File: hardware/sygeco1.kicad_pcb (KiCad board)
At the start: 2 copper layers, 57.1 x 33 mm, 12 parts, among them J1 SSD1306_module, SW1 SW_Push_DPDT, SW2 SW_Push_DPDT, U1 ATtiny85-20PU

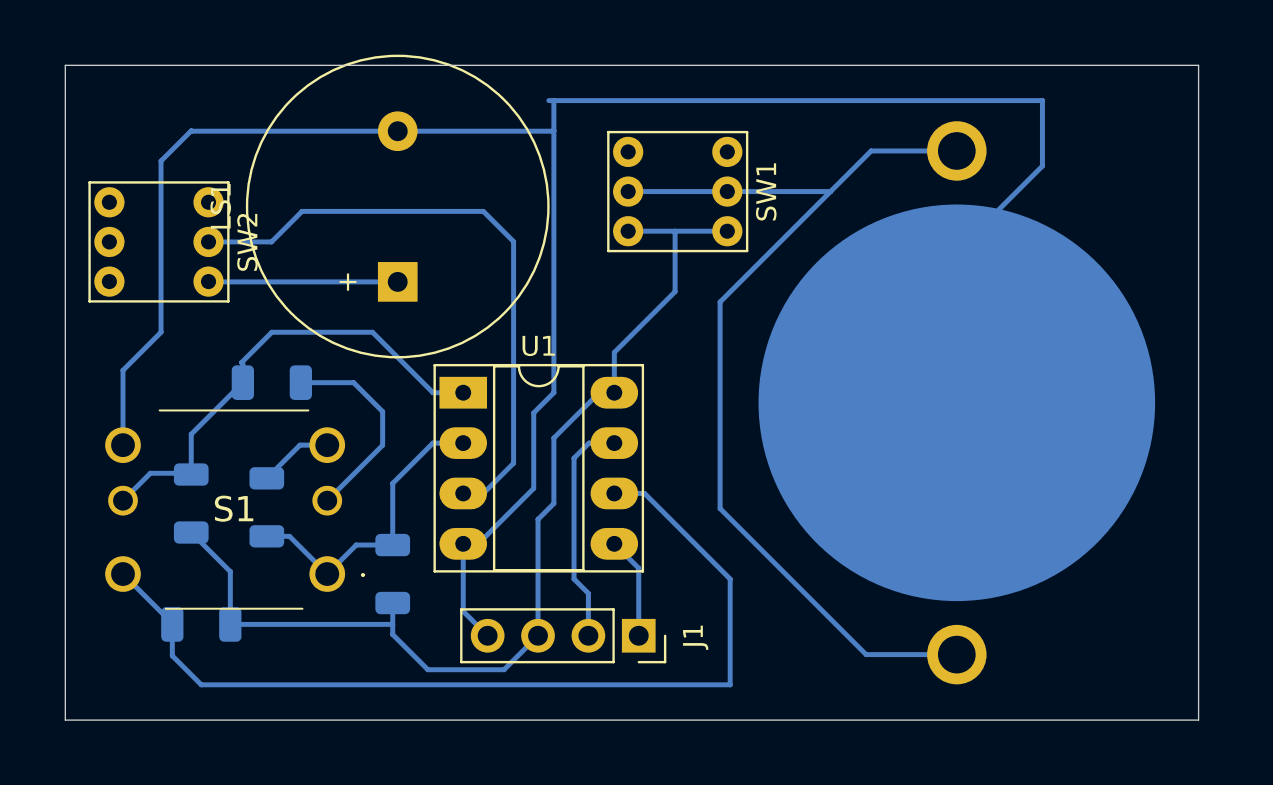
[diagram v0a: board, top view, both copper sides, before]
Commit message: add some text/logo
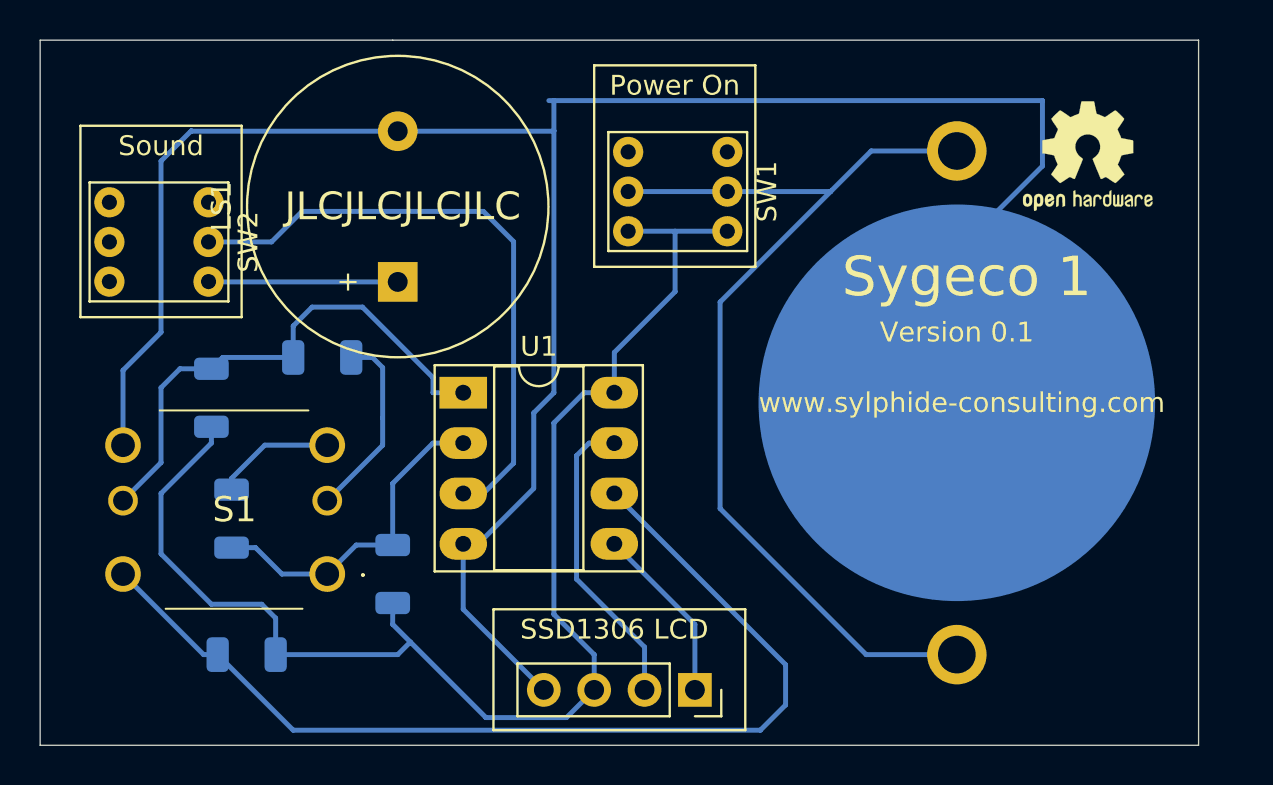
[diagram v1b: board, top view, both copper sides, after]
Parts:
- added REF**: OSHW-Logo2_7.3x6mm_SilkScreen, Symbol:OSHW-Logo2_7.3x6mm_SilkScreen, F.Cu at (177.3, 93.5)
- R3: value 50k -> 33k
- moved R1 5.43 mm to (133.1, 105.7)
- moved J1 3.93 mm to (157.5, 120.4)
- moved R2 2.84 mm to (138.7, 103.6)
- moved R3 2.75 mm to (134.9, 118.6)
- moved R5 1.87 mm to (134.1, 111.8)
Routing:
- net VCC: track 52.7 -> 69.6 mm
- net Button: track 46.9 -> 51.4 mm
- net GND: track 107.9 -> 111.8 mm
- net SDA: track 5.25 -> 9.05 mm
- net SCL: track 11.6 -> 15.4 mm
- net PAD_AXE_1: track 23.9 -> 26.6 mm
- net Net-(R5-Pad2): track 3.74 -> 6.09 mm
- net PAD_AXE_2: track 15.3 -> 16.8 mm
- net Net-(R2-Pad2): track 10.4 -> 9.67 mm
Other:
- board size 57.1 x 33 mm -> 58.4 x 35.6 mm
- board text added: "JLCJLCJLCJLC"
- board text added: "Power On"
- board text added: "SSD1306 LCD"
- board text added: "Sound"
- board text added: "Sygeco 1"
- board text added: "Version 0.1"
- board text added: "www.sylphide-consulting.com"

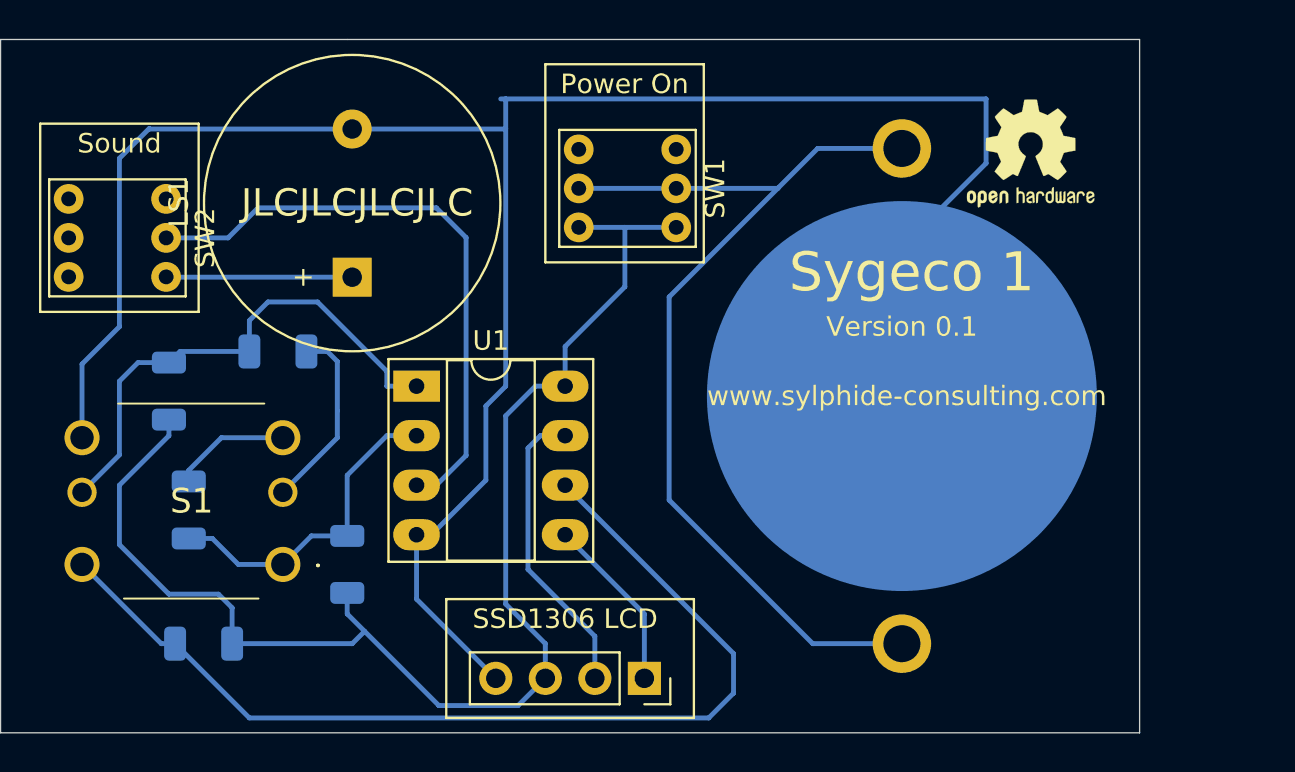
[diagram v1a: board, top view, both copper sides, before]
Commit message: keep on 'improving'. Changed beeper and cell battery holder, according to what i can get my hand on.
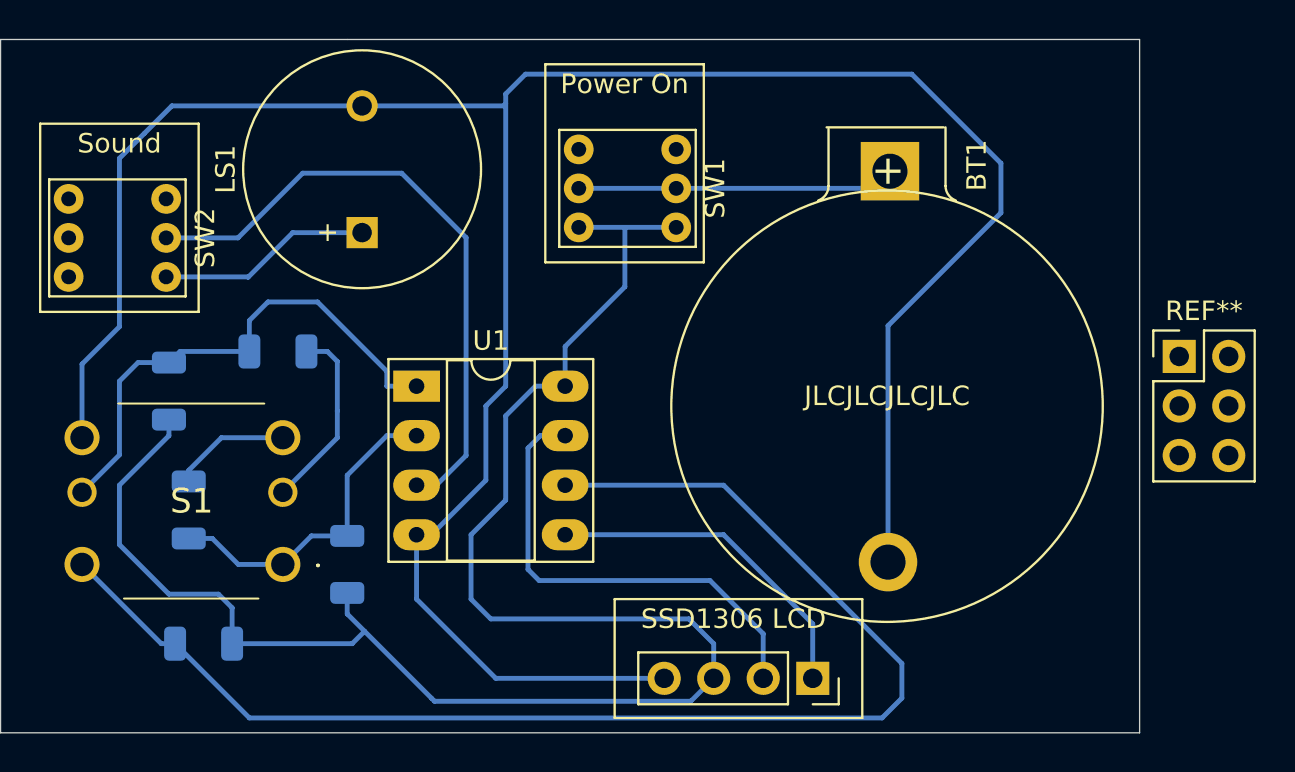
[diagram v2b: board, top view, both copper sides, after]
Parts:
- added G***: LOGO, sygeco:Sylphide_logo, B.Cu at (162.1, 105.9)
- added REF**: PinHeader_2x03_P2.54mm_Vertical, Connector_PinHeader_2.54mm:PinHeader_2x03_P2.54mm_Vertical, F.Cu at (184.9, 103.9)
- BT1: footprint Battery:BatteryHolder_Keystone_3009_1x2450 -> sygeco:BatteryHolder_China_1x20mm; moved to F.Cu
- LS1: footprint Buzzer_Beeper:Buzzer_15x7.5RM7.6 -> Buzzer_Beeper:MagneticBuzzer_ProSignal_ABT-410-RC
- REF**: moved to B.Cu
- moved REF** 23.9 mm to (176.5, 117.3), turned to 180 degrees
- moved BT1 14.8 mm to (169.9, 91.2)
- moved J1 8.64 mm to (166.1, 120.4)
- moved LS1 2.34 mm to (143.0, 97.5)
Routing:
- net Net-(BT1-Pad1): track 50.7 -> 16.3 mm
- net VCC: track 69.6 -> 89.1 mm
- net GND: track 111.8 -> 129.8 mm
- net Button: track 51.4 -> 68.6 mm
- net SCL: track 15.4 -> 24.1 mm
- net SDA: track 9.05 -> 17.4 mm
- net Net-(LS1-Pad1): track 9.55 -> 11.0 mm
- net Net-(SW2-Pad2): track 31.0 -> 32.5 mm

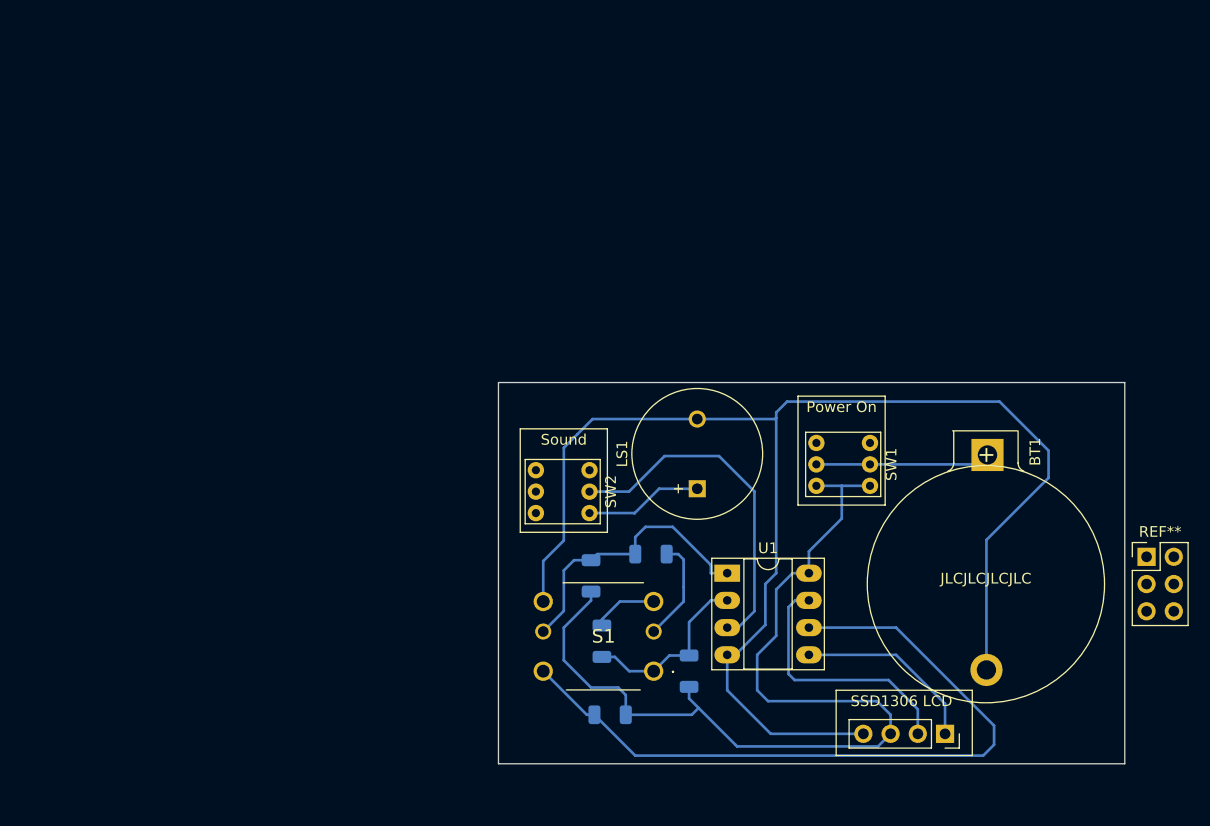
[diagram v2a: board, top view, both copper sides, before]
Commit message: add an ISP header, a power led, and redo completely the routing: * the board is bigger, but hopefully more 'practical' to use * using two layers of copper. it's the same price, why bother ?
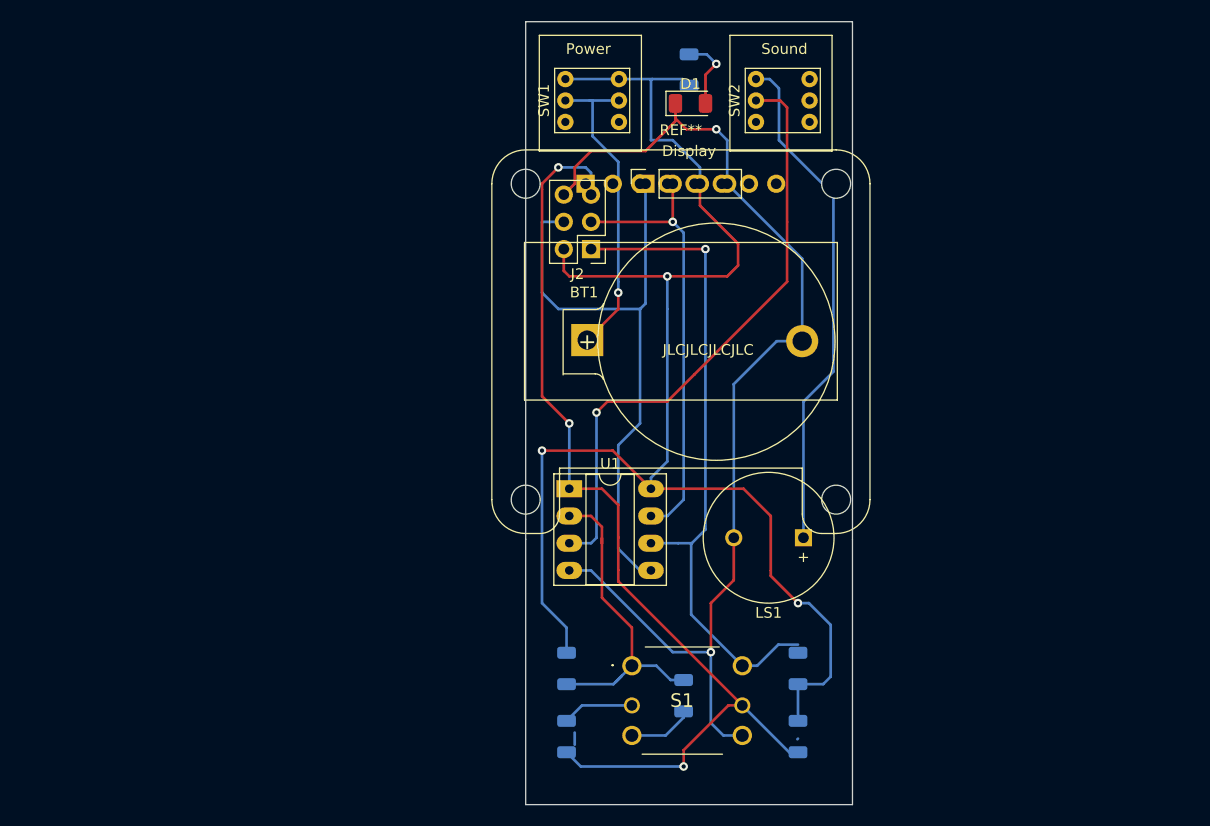
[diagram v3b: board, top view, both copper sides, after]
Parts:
- removed the REF** at (184.9, 103.9)
- added D1: LED, LED_SMD:LED_1206_3216Metric, F.Cu at (142.4, 61.6)
- added J2: AVR-ISP-6, Connector_PinHeader_2.54mm:PinHeader_2x03_P2.54mm_Vertical, F.Cu at (133.1, 75.2)
- added R6: 15, Resistor_SMD:R_1206_3216Metric, B.Cu at (142.2, 58.5)
- added REF**: Adafruit_SSD1306, Display:Adafruit_SSD1306, F.Cu at (132.6, 69.1)
- moved REF** 63.4 mm to (142.2, 64.0), turned to 270 degrees
- moved J1 58.4 mm to (138.2, 69.1), turned to 90 degrees
- moved SW2 51.0 mm to (157.5, 60.3), turned to 90 degrees
- moved BT1 41.1 mm to (129.5, 83.8), turned to 0 degrees
- moved SW1 37.4 mm to (139.7, 60.3), turned to 90 degrees
- moved G*** 33.3 mm to (149.9, 74.9), turned to 270 degrees
- moved R1 24.4 mm to (152.4, 120.7), turned to 270 degrees
- moved R2 18.8 mm to (130.8, 120.7), turned to 90 degrees
- moved R3 18.1 mm to (152.4, 114.3), turned to 90 degrees
- moved U1 16.7 mm to (131.1, 97.5)
- moved R4 11.4 mm to (130.8, 114.3), turned to 270 degrees
- moved LS1 10.9 mm to (152.9, 102.1), turned to 180 degrees
- moved R5 9.16 mm to (141.7, 116.8), turned to 270 degrees
- moved S1 2.09 mm to (136.9, 114.0), turned to 0 degrees
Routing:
- net PAD_AXE_1: track 26.6 -> 94.1 mm, vias 0 -> 3
- net VCC: track 89.1 -> 141.5 mm, vias 0 -> 3
- net SDA: track 17.4 -> 57.4 mm
- net Net-(LS1-Pad1): track 11.0 -> 47.7 mm
- net GND: track 129.8 -> 103.4 mm, vias 0 -> 2
- net Net-(SW2-Pad2): track 32.5 -> 56.7 mm, vias 0 -> 1
- net SCL: track 24.1 -> 41.2 mm, vias 0 -> 1
- net PAD_AXE_2: track 16.8 -> 32.1 mm
- net Net-(BT1-Pad1): track 16.3 -> 30.8 mm, vias 0 -> 1
- net Net-(D1-Pad2): track 0.00 -> 7.01 mm, vias 0 -> 1
- net Button: track 68.6 -> 61.9 mm, vias 0 -> 1
- net Net-(R2-Pad2): track 9.67 -> 7.26 mm
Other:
- board size 58.4 x 35.6 mm -> 30.5 x 73 mm
- board text added: "Display"
- board text added: "Power"
- board text removed: "Power On"
- board text removed: "SSD1306 LCD"

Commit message: add decoupling capacitor, use same value for keypad resistors, it's simpler
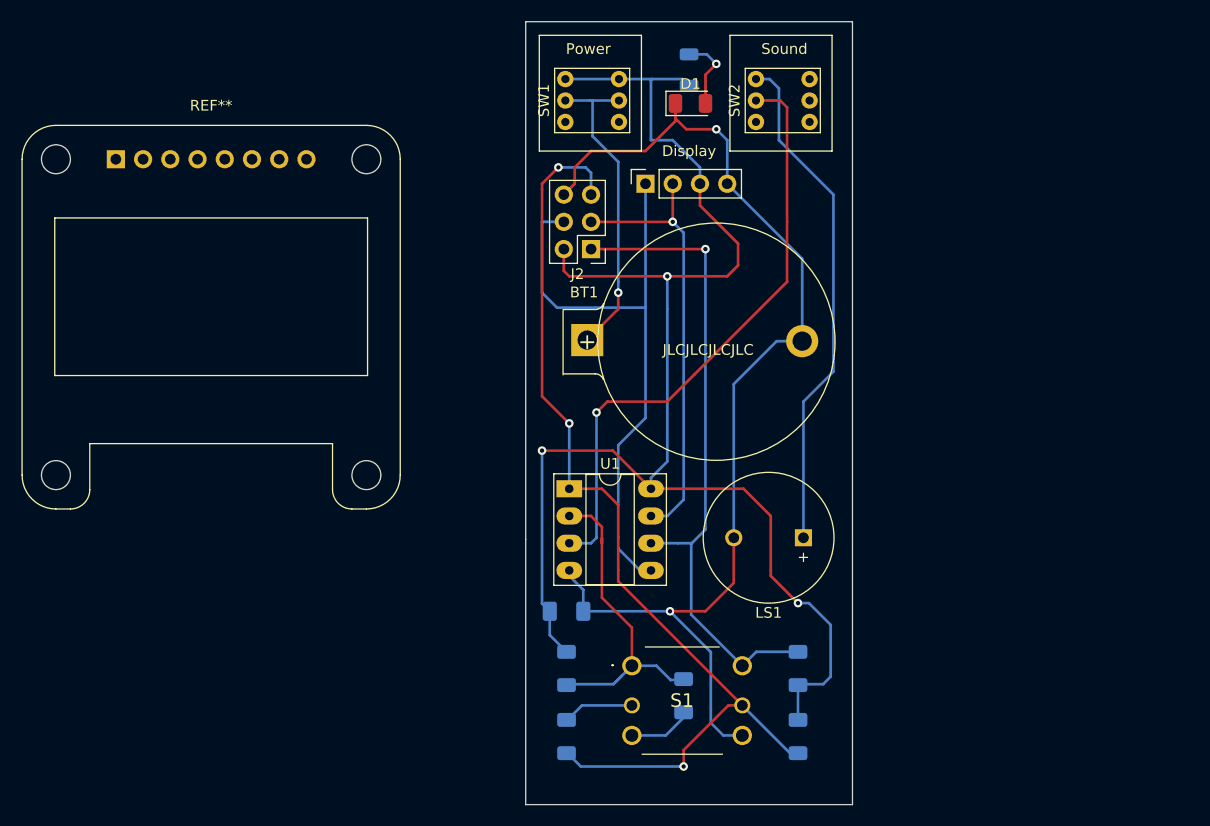
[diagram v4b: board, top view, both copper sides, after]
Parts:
- added C1: 0.1 uF, Capacitor_SMD:C_1206_3216Metric_Pad1.33x1.80mm_HandSolder, B.Cu at (130.8, 109.0)
- R1, R2, R4, R5: value 100k -> 50k; footprint Resistor_SMD:R_1206_3216Metric -> Resistor_SMD:R_1206_3216Metric_Pad1.30x1.75mm_HandSolder
- R3: value 33k -> 50k; footprint Resistor_SMD:R_1206_3216Metric -> Resistor_SMD:R_1206_3216Metric_Pad1.30x1.75mm_HandSolder
- moved REF** 43.9 mm to (88.8, 66.8)
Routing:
- net PAD_AXE_1: track 94.1 -> 92.8 mm
- net GND: track 103.4 -> 104.6 mm
